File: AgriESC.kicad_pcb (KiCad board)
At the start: 2 copper layers, 91.9 x 64 mm, 312 parts, among them J1 SUPPLY, J10 GPIO, J11 USB_OTG, J12 HALL_ENC, J2 PH_A, J3 PH_B, J4 PH_C, J6 COMM, J7 SERVO, J8 CAN, J9 SWD, SW1 SW_SPDT, U1 FDMS7698, U10 STM32F405RGT6, U11 DRV8303, U12 TJA1051TK-3, U13 LMR16006YQ, U14 MCP1700-3302E_SOT23, U15 MCP1700-3302E_SOT23, U2 FDMS7698, U3 FDMS7698, U4 FDMS7698, U5 FDMS7698, U6 FDMS7698, U7 MAX9920, U8 MAX9920, U9 MAX9920, Y1 8M Resonator

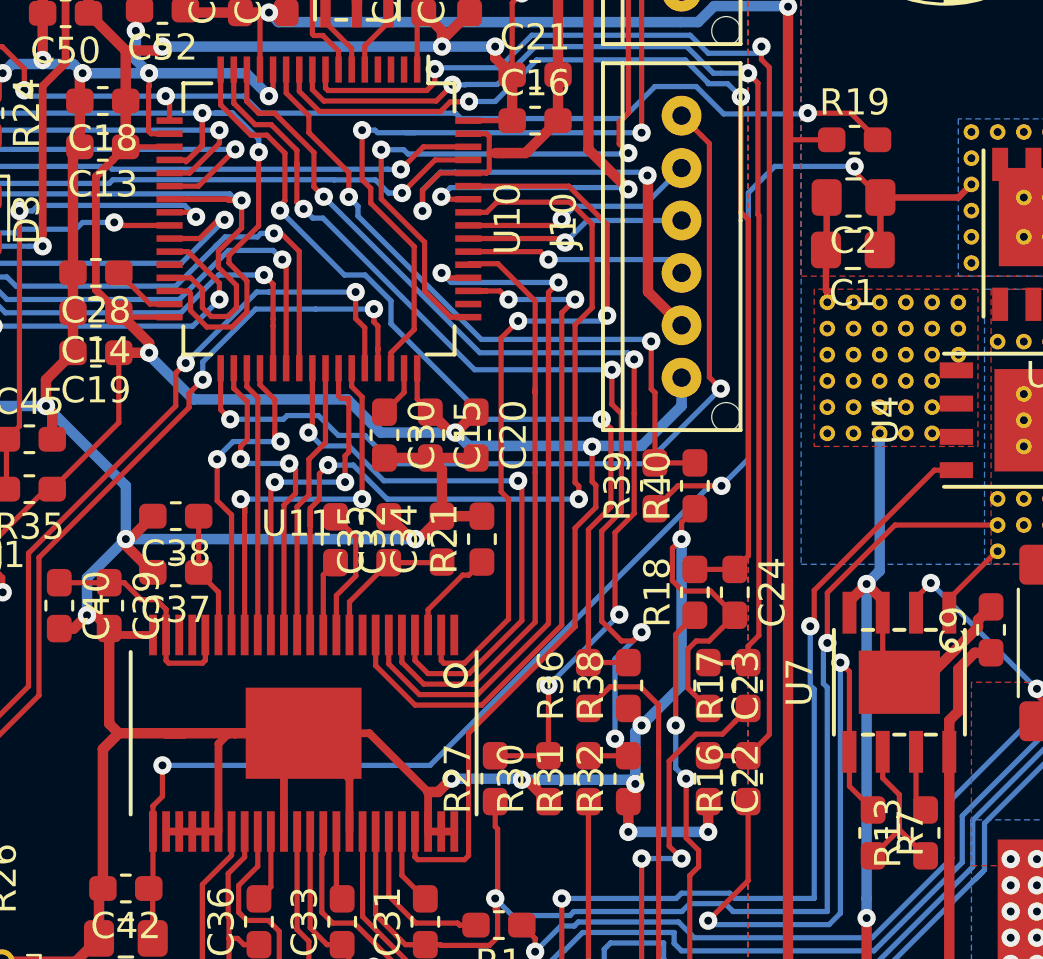
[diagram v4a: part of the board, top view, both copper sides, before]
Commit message: Stronger traces. Saving progress before trying to reduce board height
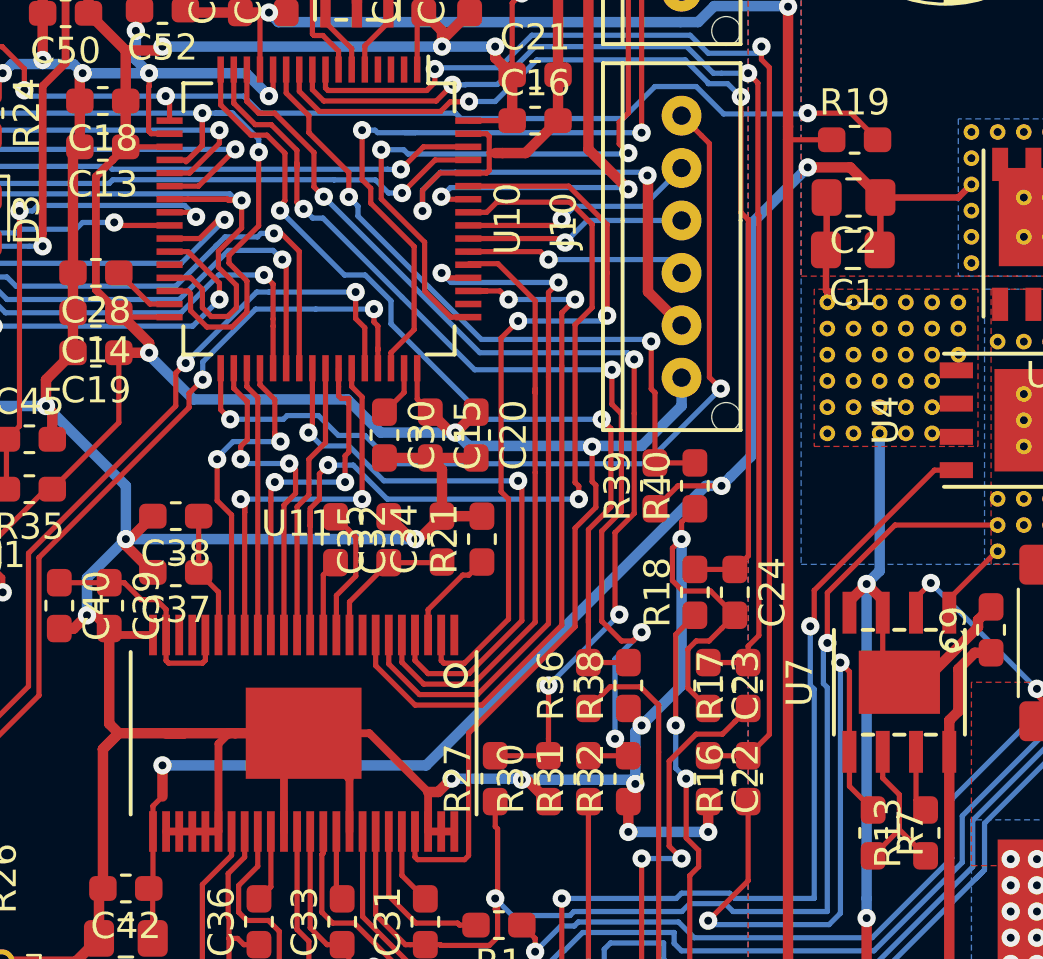
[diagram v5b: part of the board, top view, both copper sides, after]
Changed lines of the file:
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@@
     (thickness 1.6)
     (drawings 24)
-    (tracks 1910)
+    (tracks 1911)
     (zones 0)
     (modules 312)
@@
   )
   (setup
-    (last_trace_width 0.2)
+    (last_trace_width 0.4)
     (user_trace_width 0.2)
     (user_trace_width 0.3)
@@
   (segment (start 139.282 68.593) (end 141.427 68.593) (width 0.4) (layer F.Cu) (net 2))
   (via (at 129.376 112.422) (size 0.7) (drill 0.3) (layers F.Cu B.Cu) (net 2))
-  (segment (start 129.376 113.609) (end 129.376 112.422) (width 0.2) (layer F.Cu) (net 2))
   (segment (start 129.014 113.971) (end 129.376 113.609) (width 0.2) (layer F.Cu) (net 2))
   (segment (start 129.014 114.946) (end 129.014 113.971) (width 0.2) (layer F.Cu) (net 2))
   (segment (start 150.257998 101.754) (end 150.712 101.754) (width 0.2) (layer B.Cu) (net 2))
   (via (at 150.712 101.754) (size 0.7) (drill 0.3) (layers F.Cu B.Cu) (net 2))
-  (segment (start 139.589998 112.422) (end 150.257998 101.754) (width 0.2) (layer B.Cu) (net 2))
-  (segment (start 129.376 112.422) (end 139.589998 112.422) (width 0.2) (layer B.Cu) (net 2))
   (segment (start 149.047 101.754) (end 148.172 102.629) (width 0.2) (layer F.Cu) (net 2))
   (segment (start 150.712 101.754) (end 149.047 101.754) (width 0.2) (layer F.Cu) (net 2))
-  (segment (start 151.738001 100.727999) (end 151.738001 95.139999) (width 0.2) (layer B.Cu) (net 2))
-  (segment (start 150.712 101.754) (end 151.738001 100.727999) (width 0.2) (layer B.Cu) (net 2))
-  (segment (start 151.738001 95.139999) (end 151.738001 90.567999) (width 0.2) (layer B.Cu) (net 2))
-  (via (at 155.792 89.562) (size 0.7) (drill 0.3) (layers F.Cu B.Cu) (net 2))
-  (segment (start 152.744 89.562) (end 155.792 89.562) (width 0.2) (layer B.Cu) (net 2))
-  (segment (start 151.738001 90.567999) (end 152.744 89.562) (width 0.2) (layer B.Cu) (net 2))
-  (segment (start 155.792 89.767) (end 156.775 90.75) (width 0.2) (layer F.Cu) (net 2))
-  (segment (start 155.792 89.562) (end 155.792 89.767) (width 0.2) (layer F.Cu) (net 2))
   (via (at 142.584 71.782) (size 0.7) (drill 0.3) (layers F.Cu B.Cu) (net 2))
   (segment (start 143.332 71.034) (end 142.584 71.782) (width 0.4) (layer F.Cu) (net 2))
@@
   (segment (start 156.75 78.25) (end 153.25 78.25) (width 0.4) (layer F.Cu) (net 2))
   (segment (start 152.5 77.5) (end 152.5 73.298) (width 0.4) (layer F.Cu) (net 2))
+  (via (at 154.002 89.6) (size 0.7) (drill 0.3) (layers F.Cu B.Cu) (net 2))
+  (segment (start 155.625 89.6) (end 154.002 89.6) (width 0.4) (layer F.Cu) (net 2))
+  (segment (start 156.775 90.75) (end 155.625 89.6) (width 0.4) (layer F.Cu) (net 2))
+  (segment (start 151.061999 101.404001) (end 150.712 101.754) (width 0.4) (layer B.Cu) (net 2))
+  (segment (start 151.838001 100.627999) (end 151.061999 101.404001) (width 0.4) (layer B.Cu) (net 2))
+  (segment (start 151.838001 91.763999) (end 151.838001 100.627999) (width 0.4) (layer B.Cu) (net 2))
+  (segment (start 154.002 89.6) (end 151.838001 91.763999) (width 0.4) (layer B.Cu) (net 2))
+  (segment (start 150.217026 101.754) (end 150.712 101.754) (width 0.4) (layer B.Cu) (net 2))
+  (segment (start 150.109998 101.754) (end 150.217026 101.754) (width 0.4) (layer B.Cu) (net 2))
+  (segment (start 139.441998 112.422) (end 150.109998 101.754) (width 0.4) (layer B.Cu) (net 2))
+  (segment (start 129.376 112.422) (end 139.441998 112.422) (width 0.4) (layer B.Cu) (net 2))
+  (segment (start 129.376 113.609) (end 129.376 112.422) (width 0.4) (layer F.Cu) (net 2))
   (segment (start 171.905 110.7045) (end 171.905 111.9045) (width 0.4) (layer F.Cu) (net 3) (status 20))
   (segment (start 172.25 108.8) (end 172.25 110.3595) (width 0.4) (layer F.Cu) (net 3))
@@
   (segment (start 146.489999 99.563999) (end 146.14 99.214) (width 0.2) (layer F.Cu) (net 83))
   (segment (start 137.110001 93.707999) (end 138.098001 94.695999) (width 0.2) (layer B.Cu) (net 83))
-  (segment (start 145.632 106.975) (end 145.632 103.4237) (width 0.2) (layer F.Cu) (net 83))
   (segment (start 133.700057 91.221494) (end 133.836625 91.221494) (width 0.2) (layer F.Cu) (net 83))
   (segment (start 133.362571 88.369989) (end 132.752289 88.369989) (width 0.2) (layer F.Cu) (net 83))
@@
   (segment (start 138.098001 95.571999) (end 141.740002 99.214) (width 0.2) (layer B.Cu) (net 83))
   (segment (start 141.740002 99.214) (end 146.14 99.214) (width 0.2) (layer B.Cu) (net 83))
+  (segment (start 145.632 106.975) (end 145.632 103.4237) (width 0.2) (layer F.Cu) (net 83))
   (via (at 136.488 90.727906) (size 0.7) (drill 0.3) (layers F.Cu B.Cu) (net 84))
   (via (at 148.029469 96.241755) (size 0.7) (drill 0.3) (layers F.Cu B.Cu) (net 84))

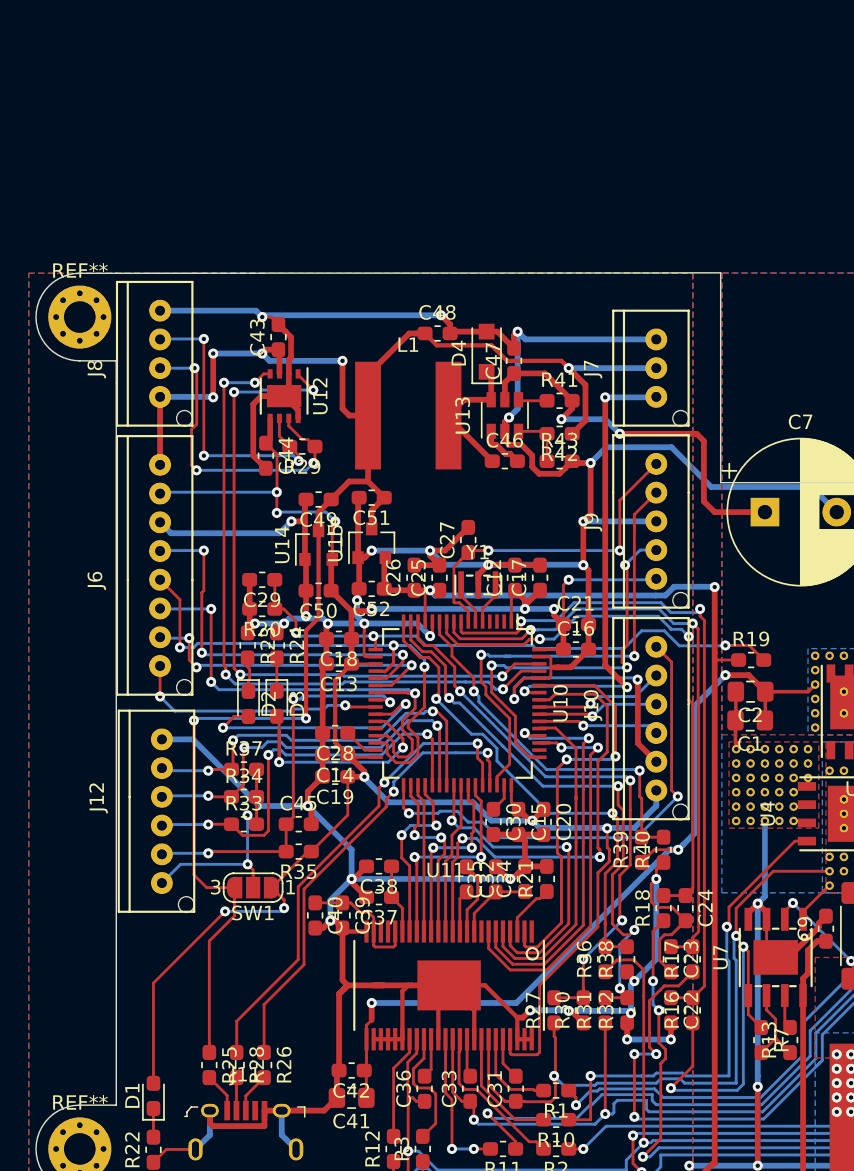
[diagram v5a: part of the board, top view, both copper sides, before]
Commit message: Trying to make board more compact by moving buck converter
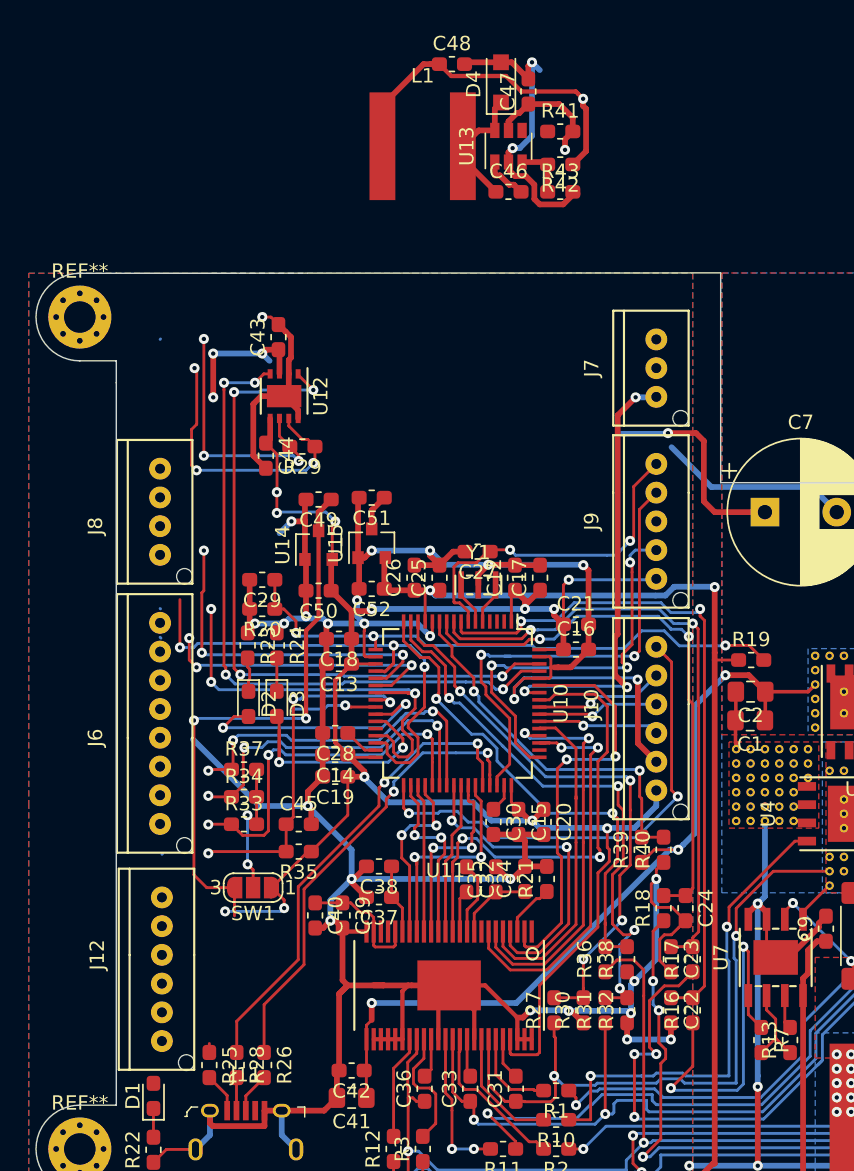
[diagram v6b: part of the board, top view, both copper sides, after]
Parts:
- moved L1 18.8 mm to (132.9, 52.8)
- moved C47 18.8 mm to (140.3, 49.0)
- moved C48 18.8 mm to (135.0, 47.1)
- moved D4 18.8 mm to (138.4, 48.3)
- moved U13 18.8 mm to (138.9, 52.8)
- moved C46 18.8 mm to (138.9, 56.0)
- moved R42 18.8 mm to (142.5, 54.0)
- moved R43 18.8 mm to (142.5, 56.0)
- moved R41 18.7 mm to (142.5, 51.8)
- moved J12 11.0 mm to (114.8, 109.1)
- moved J6 11.0 mm to (114.6, 94.0)
- moved J8 11.0 mm to (114.6, 79.2)
- moved C27 1.04 mm to (136.8, 81.0), turned to 180 degrees
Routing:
- net SL_A: track 528.3 -> 467.1 mm, vias 41 -> 38
- net +5V: track 121.3 -> 77.2 mm, vias 7 -> 6
- net VCC: track 157.7 -> 135.5 mm
- net ADC_15: track 17.8 -> 6.12 mm, vias 2 -> 1
- net Net-(J12-Pad6): track 16.7 -> 10.2 mm
- net SUPPLY: track 96.7 -> 92.2 mm
- net HALL_3: track 28.0 -> 24.7 mm
- net TX_SCL_MOSI: track 37.2 -> 34.0 mm
- net HALL_1: track 28.8 -> 25.6 mm
- net HALL_2: track 27.6 -> 24.3 mm
- net TEMP_MOTOR: track 28.1 -> 25.0 mm
- net SCK_ADC_EXT: track 27.2 -> 24.1 mm
- net CANL: track 21.7 -> 18.8 mm
- net CANH: track 22.3 -> 19.9 mm
- net RX_SDA_NSS: track 39.5 -> 37.6 mm
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
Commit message: Version 1.0 completed
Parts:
- removed D1: BLUE, LED_SMD:LED_0603_1608Metric_Pad1.05x0.95mm_HandSolder
- removed J10: GPIO, AgriESC:JST_PA_01x06
- removed J12: HALL_ENC, AgriESC:JST_PA_01x06
- removed J4: PH_C, Connector_Wire:SolderWirePad_1x01_SMD_5x10mm
- removed J6: COMM, AgriESC:JST_PA_01x08
- removed J7: SERVO, AgriESC:JST_PA_01x03
- removed J8: CAN, AgriESC:JST_PA_01x04
- removed J9: SWD, AgriESC:JST_PA_01x05
- removed the REF** at (194.9, 64.7)
- removed the REF** at (188.2, 103.2)
- removed the REF** at (172.8, 91.2)
- removed the REF** at (172.8, 90.2)
- removed the REF** at (172.8, 89.2)
- removed the REF** at (172.8, 88.2)
- removed the REF** at (173.8, 88.2)
- removed the REF** at (174.8, 88.2)
- removed the REF** at (175.8, 88.2)
- removed the REF** at (176.8, 88.2)
- removed the REF** at (177.8, 88.2)
- removed the REF** at (177.8, 103.2)
- removed the REF** at (188.2, 102.2)
- removed the REF** at (176.8, 103.2)
- removed the REF** at (175.8, 103.2)
- removed the REF** at (174.8, 103.2)
- removed the REF** at (173.8, 104.2)
- removed the REF** at (173.8, 103.2)
- removed the REF** at (173.8, 102.2)
- removed the REF** at (174.8, 102.2)
- removed the REF** at (175.8, 102.2)
- removed the REF** at (176.8, 102.2)
- removed the REF** at (177.8, 102.2)
- removed the REF** at (189.2, 103.2)
- removed the REF** at (177.8, 96.2)
- removed the REF** at (176.8, 96.2)
- removed the REF** at (175.8, 96.2)
- removed the REF** at (174.8, 96.2)
- removed the REF** at (173.8, 96.2)
- removed the REF** at (165.2, 88.2)
- removed the REF** at (164.2, 88.2)
- removed the REF** at (163.2, 88.2)
- removed the REF** at (162.2, 88.2)
- removed the REF** at (161.2, 88.2)
- removed the REF** at (189.2, 102.2)
- removed the REF** at (160.2, 88.2)
- removed the REF** at (160.2, 89.2)
- removed the REF** at (160.2, 90.2)
- removed the REF** at (160.2, 91.2)
- removed the REF** at (160.2, 92.2)
- removed the REF** at (160.2, 93.2)
- removed the REF** at (158.8, 99.8)
- removed the REF** at (157.8, 99.8)
- removed the REF** at (156.8, 99.8)
- removed the REF** at (155.8, 99.8)
- removed the REF** at (190.2, 103.2)
- removed the REF** at (154.8, 99.8)
- removed the REF** at (158.8, 98.8)
- removed the REF** at (157.8, 98.8)
- removed the REF** at (156.8, 98.8)
- removed the REF** at (155.8, 98.8)
- removed the REF** at (154.8, 98.8)
- removed the REF** at (158.8, 97.8)
- removed the REF** at (157.8, 97.8)
- removed the REF** at (156.8, 97.8)
- removed the REF** at (155.8, 97.8)
- removed the REF** at (190.2, 102.2)
- removed the REF** at (154.8, 97.8)
- removed the REF** at (158.8, 96.8)
- removed the REF** at (157.8, 96.8)
- removed the REF** at (156.8, 96.8)
- removed the REF** at (155.8, 96.8)
- removed the REF** at (154.8, 96.8)
- removed the REF** at (159.8, 95.8)
- removed the REF** at (158.8, 95.8)
- removed the REF** at (157.8, 95.8)
- removed the REF** at (156.8, 95.8)
- removed the REF** at (190.2, 96.2)
- removed the REF** at (155.8, 95.8)
- removed the REF** at (154.8, 95.8)
- removed the REF** at (159.8, 94.8)
- removed the REF** at (158.8, 94.8)
- removed the REF** at (157.8, 94.8)
- removed the REF** at (156.8, 94.8)
- removed the REF** at (155.8, 94.8)
- removed the REF** at (154.8, 94.8)
- removed the REF** at (165.2, 103.2)
- removed the REF** at (164.2, 103.2)
- removed the REF** at (189.2, 96.2)
- removed the REF** at (163.2, 103.2)
- removed the REF** at (162.2, 103.2)
- removed the REF** at (161.2, 104.2)
- removed the REF** at (161.2, 103.2)
- removed the REF** at (161.2, 102.2)
- removed the REF** at (165.2, 102.2)
- removed the REF** at (164.2, 102.2)
- removed the REF** at (163.2, 102.2)
- removed the REF** at (162.2, 102.2)
- removed the REF** at (165.2, 96.2)
- removed the REF** at (188.2, 96.2)
- removed the REF** at (164.2, 96.2)
- removed the REF** at (163.2, 96.2)
- removed the REF** at (162.2, 96.2)
- removed the REF** at (161.2, 96.2)
- removed the REF** at (109.1, 64.7)
- removed the REF** at (187.2, 96.2)
- removed the REF** at (194.9, 122.6)
- removed the REF** at (186.2, 96.2)
- removed the REF** at (190.2, 88.2)
- removed the REF** at (189.2, 88.2)
- removed the REF** at (188.2, 88.2)
- removed the REF** at (187.2, 88.2)
- removed the REF** at (186.2, 88.2)
- removed the REF** at (185.2, 93.2)
- removed the REF** at (185.2, 92.2)
- removed the REF** at (185.2, 91.2)
- removed the REF** at (185.2, 90.2)
- removed the REF** at (109.1, 122.6)
- removed the REF** at (185.2, 89.2)
- removed the REF** at (185.2, 88.2)
- removed the REF** at (183.8, 99.8)
- removed the REF** at (182.8, 99.8)
- removed the REF** at (181.8, 99.8)
- removed the REF** at (180.8, 99.8)
- removed the REF** at (179.8, 99.8)
- removed the REF** at (183.8, 98.8)
- removed the REF** at (182.8, 98.8)
- removed the REF** at (181.8, 98.8)
- removed the REF** at (159.8, 96.8)
- removed the REF** at (180.8, 98.8)
- removed the REF** at (179.8, 98.8)
- removed the REF** at (183.8, 97.8)
- removed the REF** at (182.8, 97.8)
- removed the REF** at (181.8, 97.8)
- removed the REF** at (180.8, 97.8)
- removed the REF** at (179.8, 97.8)
- removed the REF** at (184.8, 96.8)
- removed the REF** at (183.8, 96.8)
- removed the REF** at (182.8, 96.8)
- removed the REF** at (186.2, 104.2)
- removed the REF** at (181.8, 96.8)
- removed the REF** at (180.8, 96.8)
- removed the REF** at (179.8, 96.8)
- removed the REF** at (184.8, 95.8)
- removed the REF** at (183.8, 95.8)
- removed the REF** at (182.8, 95.8)
- removed the REF** at (181.8, 95.8)
- removed the REF** at (180.8, 95.8)
- removed the REF** at (179.8, 95.8)
- removed the REF** at (184.8, 94.8)
- removed the REF** at (186.2, 103.2)
- removed the REF** at (183.8, 94.8)
- removed the REF** at (182.8, 94.8)
- removed the REF** at (181.8, 94.8)
- removed the REF** at (180.8, 94.8)
- removed the REF** at (179.8, 94.8)
- removed the REF** at (171.2, 99.8)
- removed the REF** at (170.2, 99.8)
- removed the REF** at (169.2, 99.8)
- removed the REF** at (168.2, 99.8)
- removed the REF** at (167.2, 99.8)
- removed the REF** at (186.2, 102.2)
- removed the REF** at (171.2, 98.8)
- removed the REF** at (170.2, 98.8)
- removed the REF** at (169.2, 98.8)
- removed the REF** at (168.2, 98.8)
- removed the REF** at (167.2, 98.8)
- removed the REF** at (171.2, 97.8)
- removed the REF** at (170.2, 97.8)
- removed the REF** at (169.2, 97.8)
- removed the REF** at (168.2, 97.8)
- removed the REF** at (167.2, 97.8)
- removed the REF** at (187.2, 103.2)
- removed the REF** at (172.2, 96.8)
- removed the REF** at (171.2, 96.8)
- removed the REF** at (170.2, 96.8)
- removed the REF** at (169.2, 96.8)
- removed the REF** at (168.2, 96.8)
- removed the REF** at (167.2, 96.8)
- removed the REF** at (172.2, 95.8)
- removed the REF** at (171.2, 95.8)
- removed the REF** at (170.2, 95.8)
- removed the REF** at (169.2, 95.8)
- removed the REF** at (187.2, 102.2)
- removed the REF** at (168.2, 95.8)
- removed the REF** at (167.2, 95.8)
- removed the REF** at (172.2, 94.8)
- removed the REF** at (171.2, 94.8)
- removed the REF** at (170.2, 94.8)
- removed the REF** at (169.2, 94.8)
- removed the REF** at (168.2, 94.8)
- removed the REF** at (167.2, 94.8)
- removed the REF** at (172.8, 93.2)
- removed the REF** at (172.8, 92.2)
- removed SW1: SW_SPDT, Jumper:SolderJumper-3_P1.3mm_Open_RoundedPad1.0x1.5mm_NumberLabels
- added C: PH_C, Connector_Wire:SolderWirePad_1x01_SMD_5x10mm, F.Cu at (185.8, 131.0)
- added CAN: CAN, AgriESC:JST_PA_01x04, F.Cu at (114.6, 82.8)
- added COMM: COMM, AgriESC:JST_PA_01x08, F.Cu at (114.6, 97.2)
- added G***: LOGO3, AgriESC:LOGO3, F.Cu at (131.0, 71.0)
- added GPIO: GPIO, AgriESC:JST_PA_01x06, F.Cu at (149.2, 98.4)
- added HALL_ENC: HALL_ENC, AgriESC:JST_PA_01x06, F.Cu at (114.7, 111.8)
- added HALL_PWR: SW_SPDT, Jumper:SolderJumper-3_P1.3mm_Open_RoundedPad1.0x1.5mm_NumberLabels, F.Cu at (121.1, 111.1)
- added NT1: Net-Tie_2, NetTie:NetTie-2_SMD_Pad0.5mm, B.Cu at (157.8, 106.0)
- added NT2: Net-Tie_2, NetTie:NetTie-2_SMD_Pad0.5mm, B.Cu at (170.2, 106.0)
- added NT3: Net-Tie_2, NetTie:NetTie-2_SMD_Pad0.5mm, B.Cu at (182.8, 106.0)
- added PWR: BLUE, LED_SMD:LED_0603_1608Metric_Pad1.05x0.95mm_HandSolder, F.Cu at (114.2, 122.6)
- added REF**: MountingHole_3.2mm_M3_Pad_Via, MountingHole:MountingHole_3.2mm_M3_Pad_Via, F.Cu at (116.0, 132.0)
- added REF**: MountingHole_3.2mm_M3_Pad_Via, MountingHole:MountingHole_3.2mm_M3_Pad_Via, F.Cu at (195.0, 70.0)
- added REF**: MountingHole_3.2mm_M3_Pad_Via, MountingHole:MountingHole_3.2mm_M3_Pad_Via, F.Cu at (195.0, 132.0)
- added REF**: MountingHole_3.2mm_M3_Pad_Via, MountingHole:MountingHole_3.2mm_M3_Pad_Via, F.Cu at (116.0, 70.0)
- added REF**: OSHW-Logo_7.5x8mm_SilkScreen, Symbol:OSHW-Logo_7.5x8mm_SilkScreen, F.Cu at (195.0, 78.5)
- added SERVO: SERVO, AgriESC:JST_PA_01x03, F.Cu at (126.5, 79.8)
- added SWD: SWD, AgriESC:JST_PA_01x05, F.Cu at (149.2, 85.6)
- C7, C8: footprint Capacitor_THT:CP_Radial_D10.0mm_P5.00mm -> AgriESC:CP_Radial_D10.0mm_P5.00mm_Side_Mounted
- moved U13 31.1 mm to (140.9, 83.8)
- moved C46 31.1 mm to (140.9, 87.0)
- moved C47 31.1 mm to (142.3, 80.0)
- moved D4 31.1 mm to (140.4, 79.3)
- moved R41 31.1 mm to (144.5, 82.8)
- moved R42 31.1 mm to (144.5, 85.0)
- moved R43 31.1 mm to (144.5, 87.0)
- moved C48 30.9 mm to (134.8, 78.0)
- moved L1 30.1 mm to (134.9, 82.8)
- moved C43 15.1 mm to (120.5, 81.0), turned to 0 degrees
- moved R29 14.3 mm to (121.8, 87.7)
- moved C44 14.3 mm to (119.3, 88.3)
- moved U12 14.3 mm to (120.5, 84.2)
- moved R25 12.0 mm to (121.6, 128.2)
- moved R26 12.0 mm to (125.4, 128.2)
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- renumbered J2 to A, J3 to B
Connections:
- C1 pad 2: SL_A -> GND
- C10 pad 2: SL_A -> GND
- C11 pad 2: SL_A -> GND
- C12 pad 2: SL_A -> GND
- C13 pad 2: SL_A -> GND
- C14 pad 2: SL_A -> GND
- C15 pad 2: SL_A -> GND
- C16 pad 2: SL_A -> GND
- C17 pad 2: SL_A -> GND
- C18 pad 2: SL_A -> GND
- C19 pad 2: SL_A -> GND
- C2 pad 2: SL_A -> GND
- C20 pad 2: SL_A -> GND
- C21 pad 2: SL_A -> GND
- C22 pad 2: SL_A -> GND
- C23 pad 2: SL_A -> GND
- C24 pad 2: SL_A -> GND
- C25 pad 2: SL_A -> GND
- C26 pad 2: SL_A -> GND
- C27 pad 2: SL_A -> GND
- C28 pad 2: SL_A -> GND
- C29 pad 2: SL_A -> GND
- C3 pad 2: SL_A -> GND
- C30 pad 2: SL_A -> GND
- C34 pad 2: SL_A -> GND
- C35 pad 2: SL_A -> GND
- C37 pad 2: SL_A -> GND
- C38 pad 2: SL_A -> GND
- C39 pad 2: SL_A -> GND
- C4 pad 2: SL_A -> GND
- C40 pad 2: SL_A -> GND
- C41 pad 2: SL_A -> GND
- C42 pad 2: SL_A -> GND
- C43 pad 2: SL_A -> GND
- C44 pad 2: SL_A -> GND
- C45 pad 2: SL_A -> GND
- C47 pad 2: SL_A -> GND
- C48 pad 2: SL_A -> GND
- C49 pad 2: SL_A -> GND
- C5 pad 2: SL_A -> GND
- C50 pad 2: SL_A -> GND
- C51 pad 2: SL_A -> GND
- C52 pad 2: SL_A -> GND
- C6 pad 2: SL_A -> GND
- C7 pad 2: SL_A -> GND
- C8 pad 2: SL_A -> GND
- C9 pad 2: SL_A -> GND
- D4 pad 2: SL_A -> GND
- J1 pad 1: SL_A -> GND
- J11 pad 5: SL_A -> GND
- J11 pad 6: SL_A -> GND
- R20 pad 2: SL_A -> GND
- R21 pad 2: SL_A -> GND
- R22 pad 1: SL_A -> GND
- R23 pad 1: SL_A -> GND
- R24 pad 1: SL_A -> GND
- R30 pad 1: SL_A -> GND
- R32 pad 1: SL_A -> GND
- R33 pad 2: Net-(J12-Pad6) -> VCC
- R34 pad 2: Net-(J12-Pad6) -> VCC
- R37 pad 2: Net-(J12-Pad6) -> VCC
- R38 pad 1: SL_A -> GND
- R40 pad 1: SL_A -> GND
- R43 pad 2: SL_A -> GND
- U10 pad 12: SL_A -> GND
- U10 pad 18: SL_A -> GND
- U10 pad 60: SL_A -> GND
- U10 pad 63: SL_A -> GND
- U11 pad 24: SL_A -> GND
- U11 pad 26: SL_A -> GND
- U11 pad 27: SL_A -> GND
- U11 pad 28: SL_A -> GND
- U11 pad 29: SL_A -> GND
- U11 pad 30: SL_A -> SL_C
- U11 pad 35: SL_A -> SL_B
- U11 pad 46: SL_A -> GND
- U11 pad 47: SL_A -> GND
- U11 pad 48: SL_A -> GND
- U12 pad 2: SL_A -> GND
- U12 pad 8: SL_A -> GND
- U12 pad 9: SL_A -> GND
- U13 pad 2: SL_A -> GND
- U14 pad 1: SL_A -> GND
- U15 pad 1: SL_A -> GND
- U4 pad 3: SL_A -> GND
- U5 pad 3: SL_A -> GND
- U6 pad 3: SL_A -> GND
- U7 pad 3: SL_A -> GND
- U7 pad 4: SL_A -> GND
- U8 pad 3: SL_A -> GND
- U8 pad 4: SL_A -> GND
- U9 pad 3: SL_A -> GND
- U9 pad 4: SL_A -> GND
- Y1 pad 2: SL_A -> GND
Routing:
- net GND: track 0.00 -> 575.2 mm, vias 0 -> 235
- net SL_A: track 467.1 -> 53.6 mm, vias 38 -> 3
- net SL_C: track 0.00 -> 84.5 mm, vias 0 -> 3
- net SL_B: track 0.00 -> 69.9 mm, vias 0 -> 3
- net SUPPLY: track 92.2 -> 153.9 mm, vias 5 -> 90
- net VCC: track 135.5 -> 190.3 mm, vias 12 -> 15
- net +5V: track 77.2 -> 113.8 mm, vias 6 -> 4
- net Net-(J3-Pad1): track 19.7 -> 36.6 mm, vias 27 -> 114
- net Net-(J2-Pad1): track 18.3 -> 34.1 mm, vias 27 -> 114
- net Net-(J4-Pad1): track 19.3 -> 34.2 mm, vias 27 -> 114
- net SH_B: track 66.1 -> 80.4 mm, vias 3 -> 35
- net SERVO: track 31.0 -> 44.2 mm
- net C_A: track 26.2 -> 13.0 mm
- net Net-(R1-Pad1): track 43.8 -> 56.3 mm, vias 2 -> 6
- net Net-(R11-Pad1): track 49.2 -> 61.5 mm, vias 2 -> 4
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- added copper zone on B.Cu, net GND
- added copper zone on F.Cu, net GND
- removed copper zone on B.Cu, net SL_A
- removed copper zone on F.Cu, net SL_A
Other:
- board size 91.9 x 64 mm -> 89 x 72 mm
- board text added: "2018-12-15 github.com/norn93/AgriESC georgeknowlden.com"
- board text added: "24 V, 36 V max 10 A, 25 A max"
- board text added: "AgriESC 1.0"
